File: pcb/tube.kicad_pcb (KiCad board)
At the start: 2 copper layers, 99.1 x 116.8 mm, 80 parts, among them J1 Screw_Terminal_01x02, J10 LED_[5..8], J11 LED_[1..4], J2 Screw_Terminal_01x02, J3 Screw_Terminal_01x02, J4 Conn_01x04_Pin, J5 Conn_01x08_Pin, J6 Conn_01x05_Pin, U1 INA226, U10 74LS32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

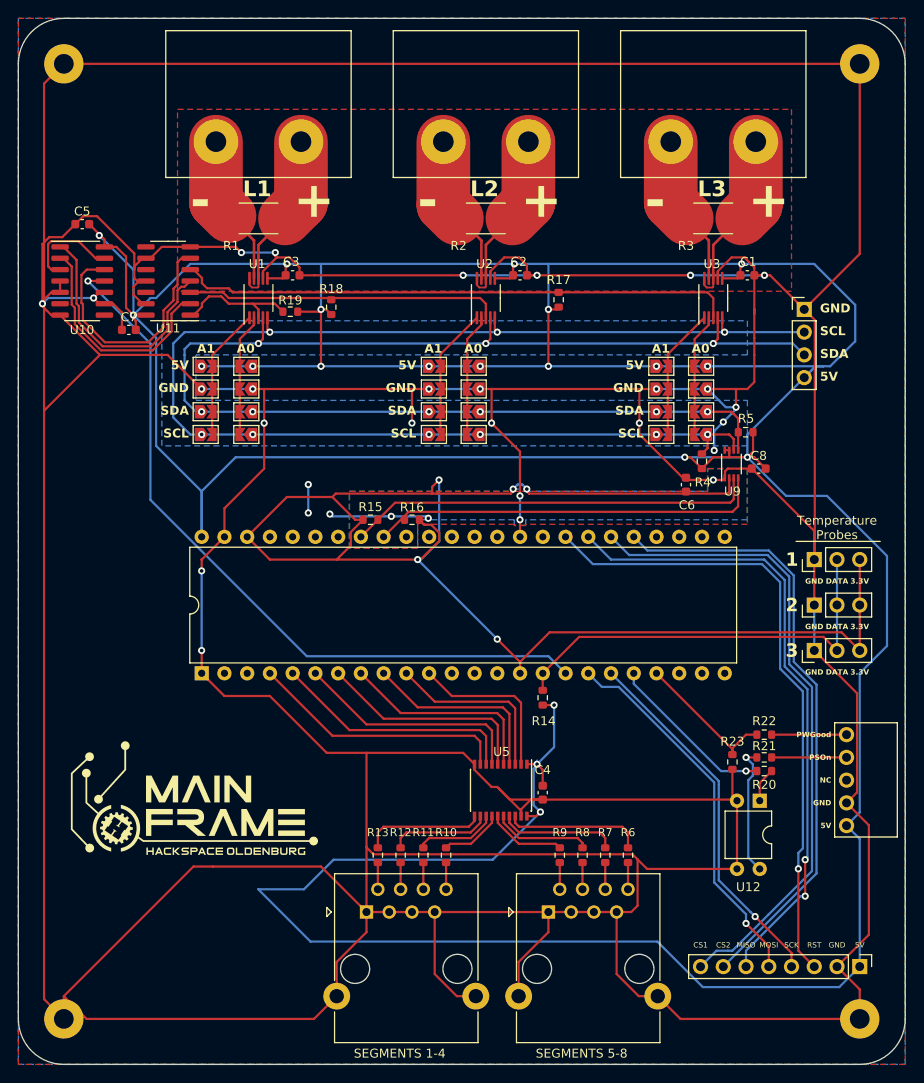
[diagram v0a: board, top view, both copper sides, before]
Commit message: PCB: Use 0805
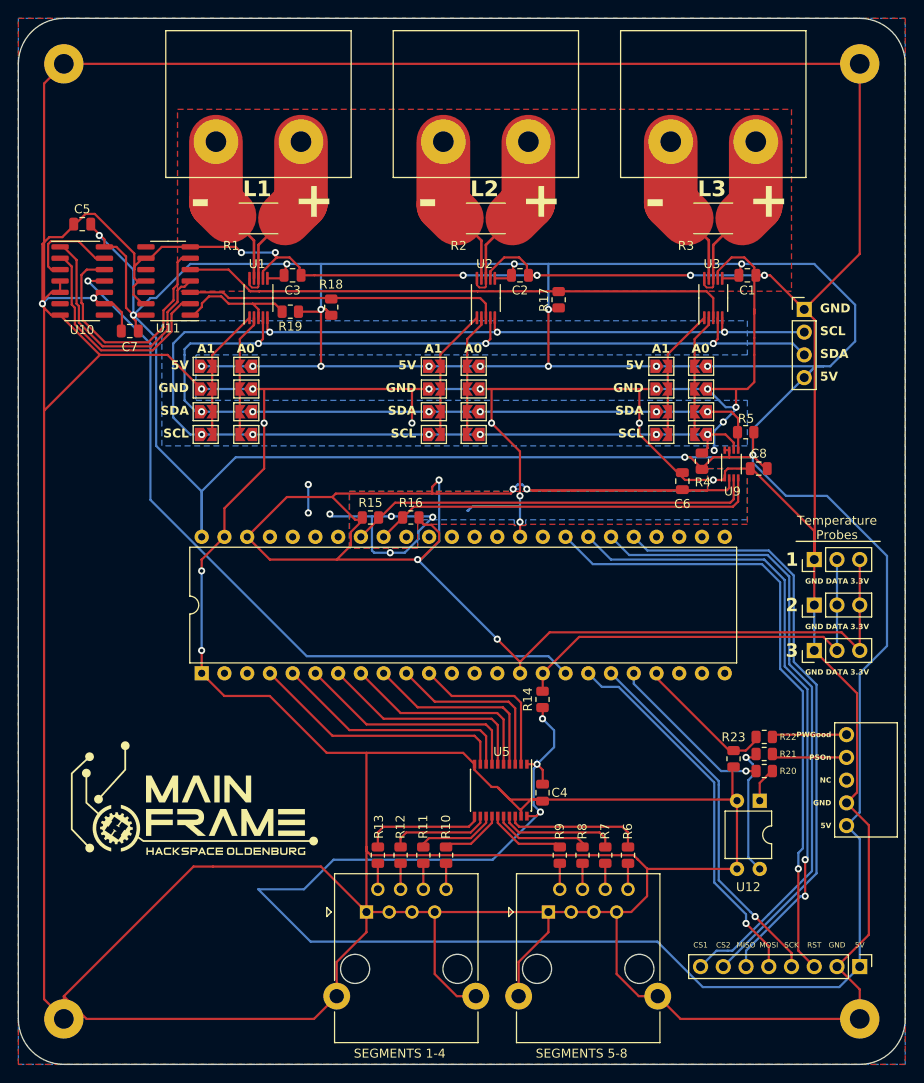
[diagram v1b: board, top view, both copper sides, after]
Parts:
- C1, C2, C3, C4, C5, C6, C7, C8: footprint Capacitor_SMD:C_0603_1608Metric -> Capacitor_SMD:C_0805_2012Metric
- R10, R11, R12, R13, R14, R15, R16, R17, R18, R19, R20, R21, R22, R23, R4, R5, R6, R7, R8, R9: footprint Resistor_SMD:R_0603_1608Metric -> Resistor_SMD:R_0805_2012Metric
- moved C6 0.56 mm to (216.4, 155.8)
- moved R21 0.38 mm to (225.6, 186.3)
- moved R23 0.38 mm to (222.1, 186.8)
- moved R16 0.28 mm to (186.1, 159.9)
- moved R22 0.25 mm to (225.6, 184.4)
- moved R15 0.25 mm to (181.6, 159.9)
- moved R14 0.19 mm to (200.8, 180.2)
- moved C7 0.17 mm to (154.7, 139.1)
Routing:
- net GND: track 1007.0 -> 1026.6 mm, vias 31 -> 32
- net +5V: track 552.5 -> 551.7 mm
- net +3.3V: track 176.1 -> 175.4 mm
- net Net-(U4-29_TX7): track 16.7 -> 16.1 mm

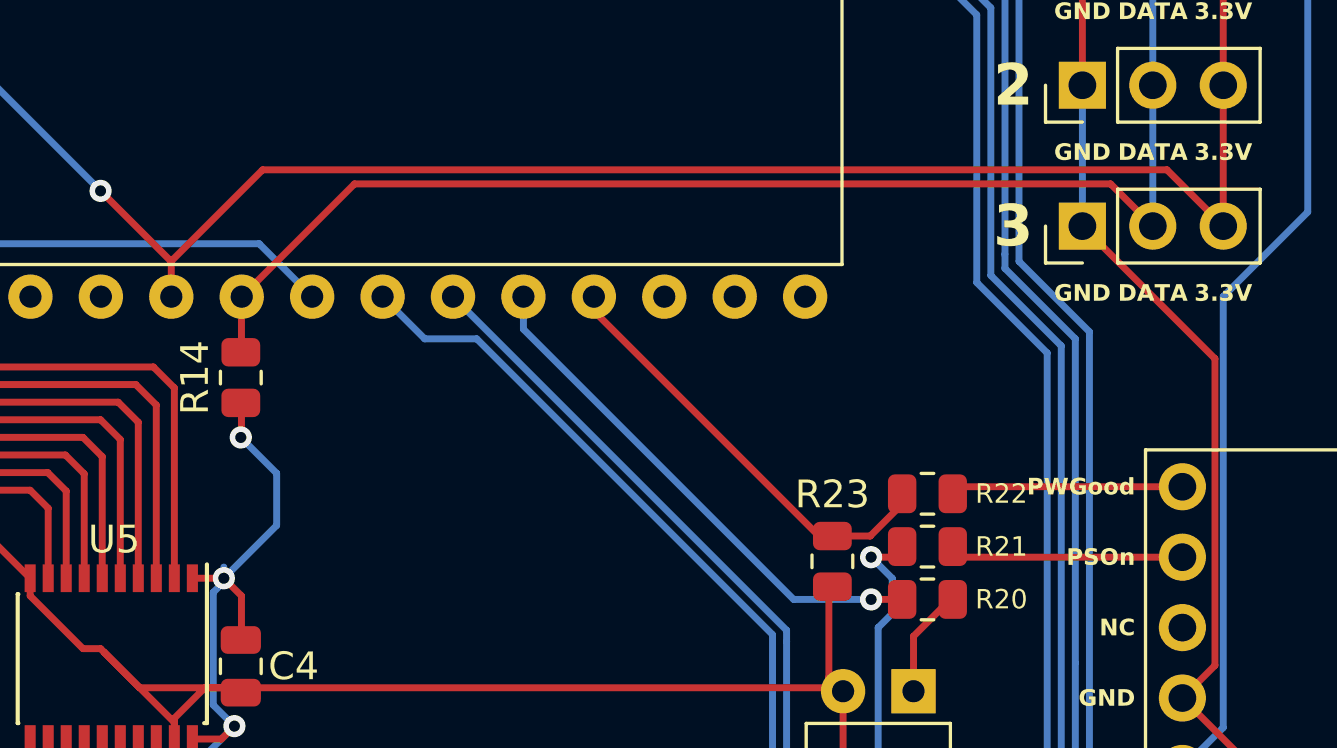
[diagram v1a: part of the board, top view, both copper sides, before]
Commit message: PCB: Verify Pullups
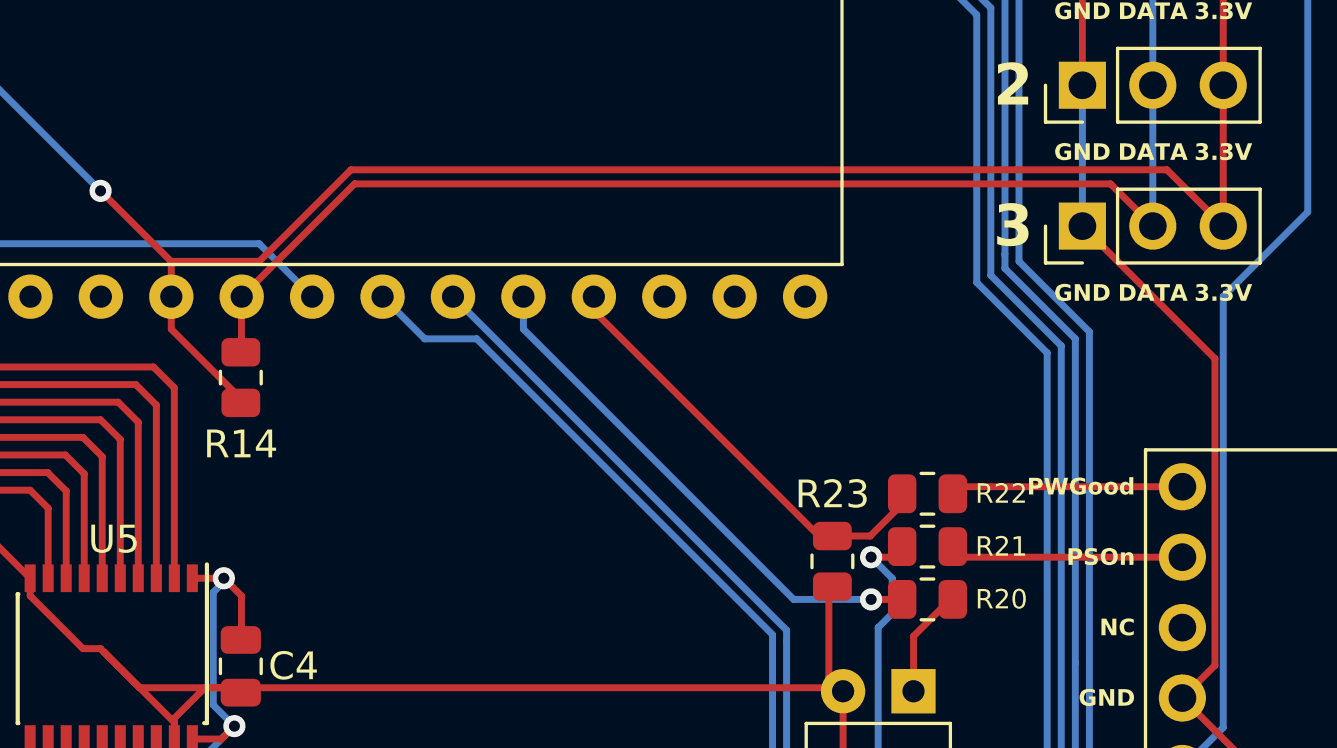
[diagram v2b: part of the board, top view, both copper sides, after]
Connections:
- R14 pad 1: +5V -> +3.3V
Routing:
- net +5V: track 551.7 -> 543.4 mm, vias 20 -> 19
- net +3.3V: track 175.4 -> 180.2 mm
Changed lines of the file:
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@@
     (property "ki_keywords" "R res resistor")
     (attr smd)
-    (fp_text reference "R14" (at 0 -1.65 90) (layer "F.SilkS")
+    (fp_text reference "R14" (at -2.413 0 180) (layer "F.SilkS")
         (effects (font (size 1 1) (thickness 0.15)))
     )
@@
       (stroke (width 0.1) (type solid)) (layer "F.Fab"))
     (pad "1" smd roundrect (at -0.9125 0 90) (size 1.025 1.4) (layers "F.Cu" "F.Paste" "F.Mask") (roundrect_rratio 0.243902)
-      (net 2 "+5V") (pintype "passive"))
+      (net 31 "+3.3V") (pintype "passive"))
     (pad "2" smd roundrect (at 0.9125 0 90) (size 1.025 1.4) (layers "F.Cu" "F.Paste" "F.Mask") (roundrect_rratio 0.243902)
       (net 27 "/TEMP") (pintype "passive"))
@@
   (segment (start 153.185 129.665) (end 151.85 129.665) (width 0.25) (layer "F.Cu") (net 2))
   (segment (start 221.636 153.162) (end 221.638 153.16) (width 0.25) (layer "F.Cu") (net 2))
-  (segment (start 200.787 182.372) (end 200.81 182.349) (width 0.25) (layer "F.Cu") (net 2))
   (segment (start 222.555 133.18) (end 222.895 132.84) (width 0.25) (layer "F.Cu") (net 2))
   (segment (start 199.04 193.25) (end 200.09 193.25) (width 0.25) (layer "F.Cu") (net 2))
@@
   (segment (start 219.858 153.162) (end 221.636 153.162) (width 0.25) (layer "F.Cu") (net 2))
   (segment (start 220.86 133.18) (end 222.555 133.18) (width 0.25) (layer "F.Cu") (net 2))
-  (segment (start 200.81 182.349) (end 200.81 180.846) (width 0.25) (layer "F.Cu") (net 2))
   (segment (start 221.642 153.156) (end 221.638 153.16) (width 0.25) (layer "F.Cu") (net 2))
   (segment (start 216.685 153.16) (end 217.32 153.16) (width 0.25) (layer "F.Cu") (net 2))
@@
   (via (at 216.685 153.16) (size 0.8) (drill 0.4) (layers "F.Cu" "B.Cu") (net 2))
   (via (at 224.282 152.908) (size 0.8) (drill 0.4) (layers "F.Cu" "B.Cu") (net 2))
-  (via (at 200.787 182.372) (size 0.8) (drill 0.4) (layers "F.Cu" "B.Cu") (net 2))
   (via (at 155.09 137.285) (size 0.8) (drill 0.4) (layers "F.Cu" "B.Cu") (net 2))
   (via (at 193.825 143) (size 0.8) (drill 0.4) (layers "F.Cu" "B.Cu") (net 2))
@@
   (segment (start 193.825 143) (end 213.51 143) (width 0.25) (layer "B.Cu") (net 2))
   (segment (start 213.51 143) (end 219.225 143) (width 0.25) (layer "B.Cu") (net 2))
-  (segment (start 200.787 182.372) (end 202.08 183.665) (width 0.25) (layer "B.Cu") (net 2))
   (segment (start 235.712 140.208) (end 235.712 136.144) (width 0.25) (layer "B.Cu") (net 2))
   (segment (start 201.445 131.57) (end 201.445 136.65) (width 0.25) (layer "B.Cu") (net 2))
@@
   (segment (start 176.045 131.57) (end 176.045 136.65) (width 0.25) (layer "B.Cu") (net 2))
   (segment (start 169.035 201.42) (end 174.14 201.42) (width 0.25) (layer "B.Cu") (net 2))
-  (segment (start 202.08 183.665) (end 202.08 185.545) (width 0.25) (layer "B.Cu") (net 2))
   (segment (start 239.268 164.188) (end 239.268 174.242) (width 0.25) (layer "B.Cu") (net 2))
   (segment (start 174.14 201.42) (end 177.442 198.118) (width 0.25) (layer "B.Cu") (net 2))
@@
   (segment (start 232.92 143) (end 235.712 140.208) (width 0.25) (layer "B.Cu") (net 2))
   (segment (start 200.175 187.45) (end 200.175 187.577) (width 0.25) (layer "B.Cu") (net 2))
-  (segment (start 200.175 187.45) (end 200.175 187.046) (width 0.25) (layer "B.Cu") (net 2))
   (segment (start 232.156 143) (end 232.92 143) (width 0.25) (layer "B.Cu") (net 2))
   (segment (start 224.282 152.908) (end 224.282 153.772) (width 0.25) (layer "B.Cu") (net 2))
-  (segment (start 202.08 185.545) (end 200.175 187.45) (width 0.25) (layer "B.Cu") (net 2))
   (segment (start 172.235 131.57) (end 176.045 131.57) (width 0.25) (layer "B.Cu") (net 2))
   (segment (start 231.29 143) (end 230.02 144.27) (width 0.25) (layer "B.Cu") (net 2))
@@
   (segment (start 197.508 156.716) (end 197.762 156.716) (width 0.25) (layer "F.Cu") (net 31))
   (segment (start 188.976 157.226) (end 188.978 157.224) (width 0.25) (layer "F.Cu") (net 31))
+  (segment (start 201.456604 176.022) (end 204.758604 172.72) (width 0.25) (layer "F.Cu") (net 31))
   (segment (start 177.315 157.605) (end 172.235 157.605) (width 0.25) (layer "F.Cu") (net 31))
   (segment (start 221.394 156.845) (end 199.161 156.845) (width 0.25) (layer "F.Cu") (net 31))
@@
   (segment (start 187.175991 164.59) (end 186.84 164.59) (width 0.25) (layer "F.Cu") (net 31))
   (segment (start 189.23 155.702) (end 188.468 156.464) (width 0.25) (layer "F.Cu") (net 31))
-  (segment (start 198.272 176.022) (end 201.574 172.72) (width 0.25) (layer "F.Cu") (net 31))
-  (segment (start 234.19 172.72) (end 236.22 174.75) (width 0.25) (layer "F.Cu") (net 31))
+  (segment (start 200.787 181.1255) (end 200.787 180.975) (width 0.25) (layer "F.Cu") (net 31))
   (segment (start 188.468 156.464) (end 188.468 157.224) (width 0.25) (layer "F.Cu") (net 31))
   (segment (start 197.762 156.716) (end 197.762 156.716) (width 0.25) (layer "F.Cu") (net 31))
   (segment (start 188.974 157.224) (end 188.976 157.226) (width 0.25) (layer "F.Cu") (net 31))
+  (segment (start 200.787 180.975) (end 198.28 178.468) (width 0.25) (layer "F.Cu") (net 31))
   (segment (start 197.508 156.97) (end 197.508 156.716) (width 0.25) (layer "F.Cu") (net 31))
   (segment (start 167.8 162.06) (end 170.332 164.592) (width 0.25) (layer "F.Cu") (net 31))
@@
   (segment (start 177.8 164.592) (end 186.838 164.592) (width 0.25) (layer "F.Cu") (net 31))
   (segment (start 177.315 157.605) (end 179.855 160.145) (width 0.25) (layer "F.Cu") (net 31))
-  (segment (start 201.574 172.72) (end 234.19 172.72) (width 0.25) (layer "F.Cu") (net 31))
   (segment (start 187.03 160.145) (end 187.5925 160.7075) (width 0.25) (layer "F.Cu") (net 31))
+  (segment (start 204.758604 172.72) (end 234.19 172.72) (width 0.25) (layer "F.Cu") (net 31))
   (segment (start 172.235 157.605) (end 167.8 162.04) (width 0.25) (layer "F.Cu") (net 31))
   (segment (start 195.73 173.48) (end 198.272 176.022) (width 0.25) (layer "F.Cu") (net 31))
   (segment (start 179.375 161.515) (end 179.375 163.017) (width 0.25) (layer "F.Cu") (net 31))
+  (segment (start 198.272 176.022) (end 201.456604 176.022) (width 0.25) (layer "F.Cu") (net 31))
   (segment (start 221.394 156.845) (end 221.642 156.597) (width 0.25) (layer "F.Cu") (net 31))
   (segment (start 236.22 174.75) (end 236.22 164.59) (width 0.25) (layer "F.Cu") (net 31))
+  (segment (start 198.28 178.468) (end 198.28 177.295) (width 0.25) (layer "F.Cu") (net 31))
   (segment (start 179.375 163.017) (end 177.8 164.592) (width 0.25) (layer "F.Cu") (net 31))
   (segment (start 177.696 157.224) (end 188.468 157.224) (width 0.25) (layer "F.Cu") (net 31))
   (segment (start 186.838 164.592) (end 186.84 164.59) (width 0.25) (layer "F.Cu") (net 31))
   (segment (start 197.254 157.224) (end 197.508 156.97) (width 0.25) (layer "F.Cu") (net 31))
+  (segment (start 234.19 172.72) (end 236.22 174.75) (width 0.25) (layer "F.Cu") (net 31))
   (via (at 195.73 173.48) (size 0.8) (drill 0.4) (layers "F.Cu" "B.Cu") (net 31))
   (via (at 197.508 156.716) (size 0.8) (drill 0.4) (layers "F.Cu" "B.Cu") (net 31))

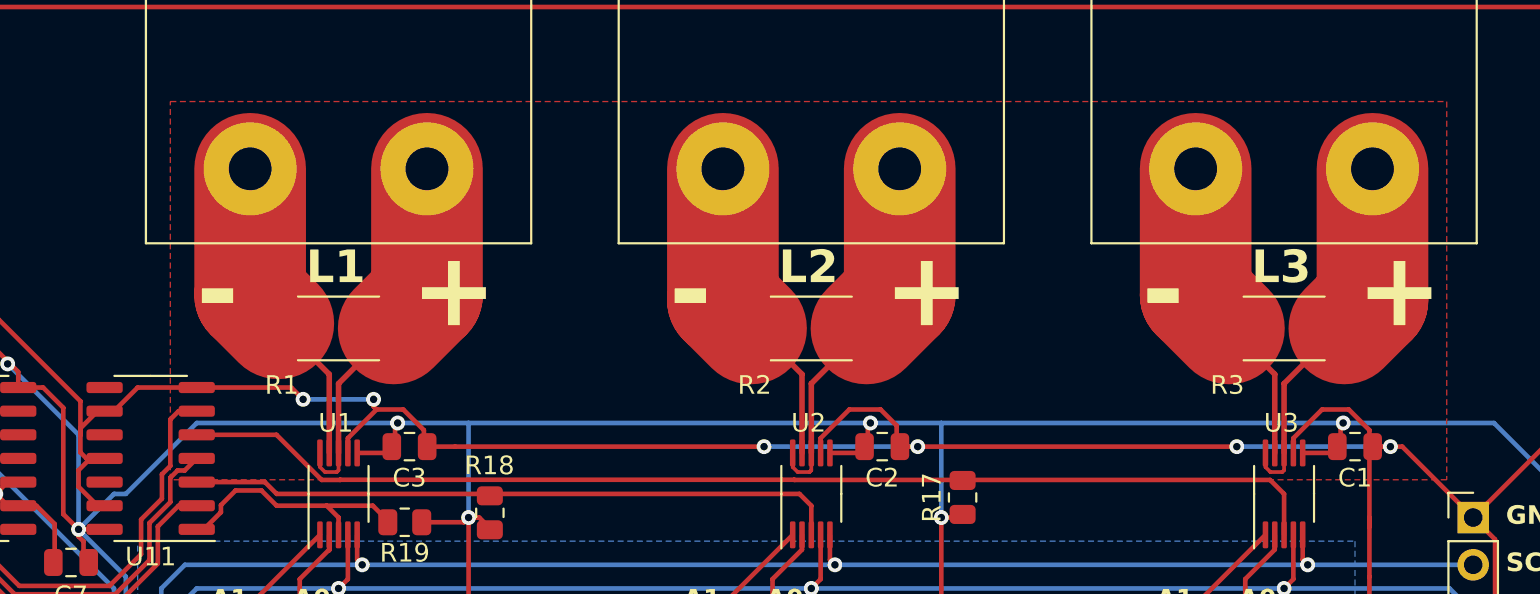
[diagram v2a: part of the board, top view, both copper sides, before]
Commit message: PCB: Tweak Shunt Traces
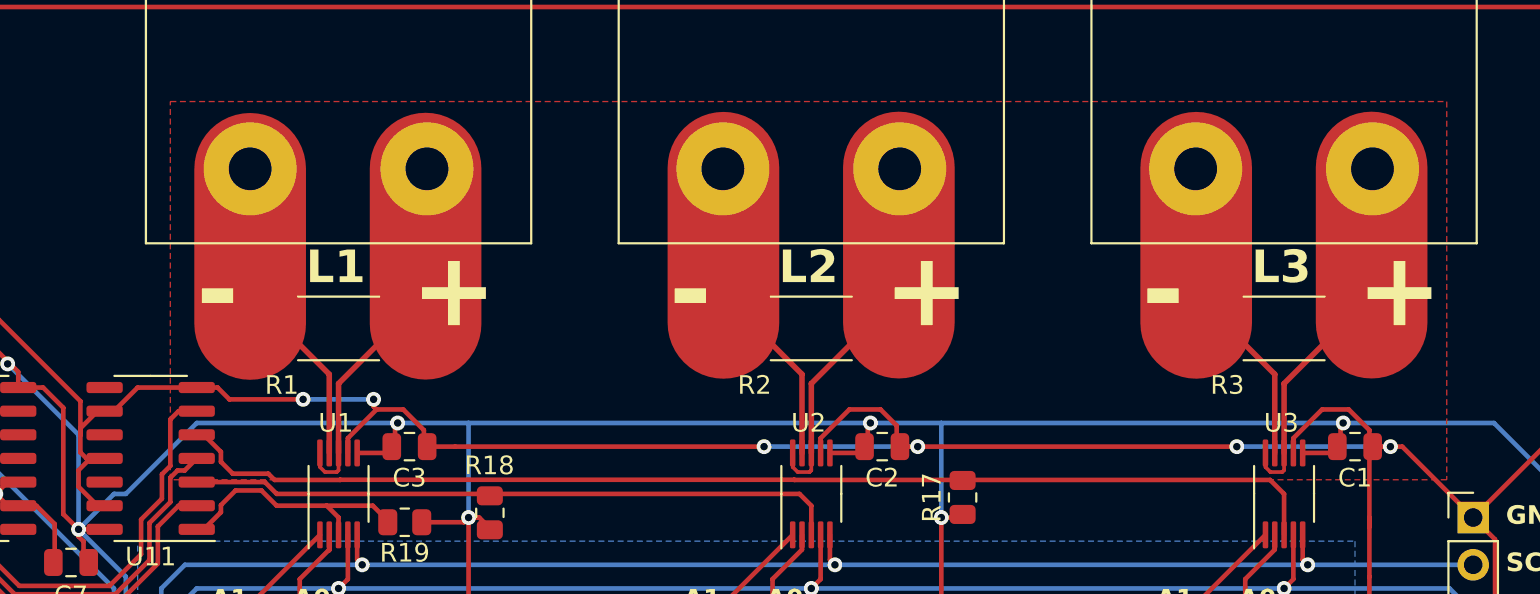
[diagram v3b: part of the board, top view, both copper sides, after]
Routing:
- net /Vin1+: track 20.1 -> 19.1 mm
- net /Vin3-: track 17.0 -> 16.0 mm
- net /Vin2+: track 20.1 -> 19.1 mm
- net /Vin3+: track 20.0 -> 19.1 mm
- net /Vin2-: track 16.9 -> 16.0 mm
- net /Vin1-: track 16.6 -> 16.0 mm
